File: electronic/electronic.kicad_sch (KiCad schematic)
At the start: 4 parts, among them M01 Brushless Motor, U1 ESC HW30A, U1 ESP32-DEVKITC-32E, U2 MPU-6050

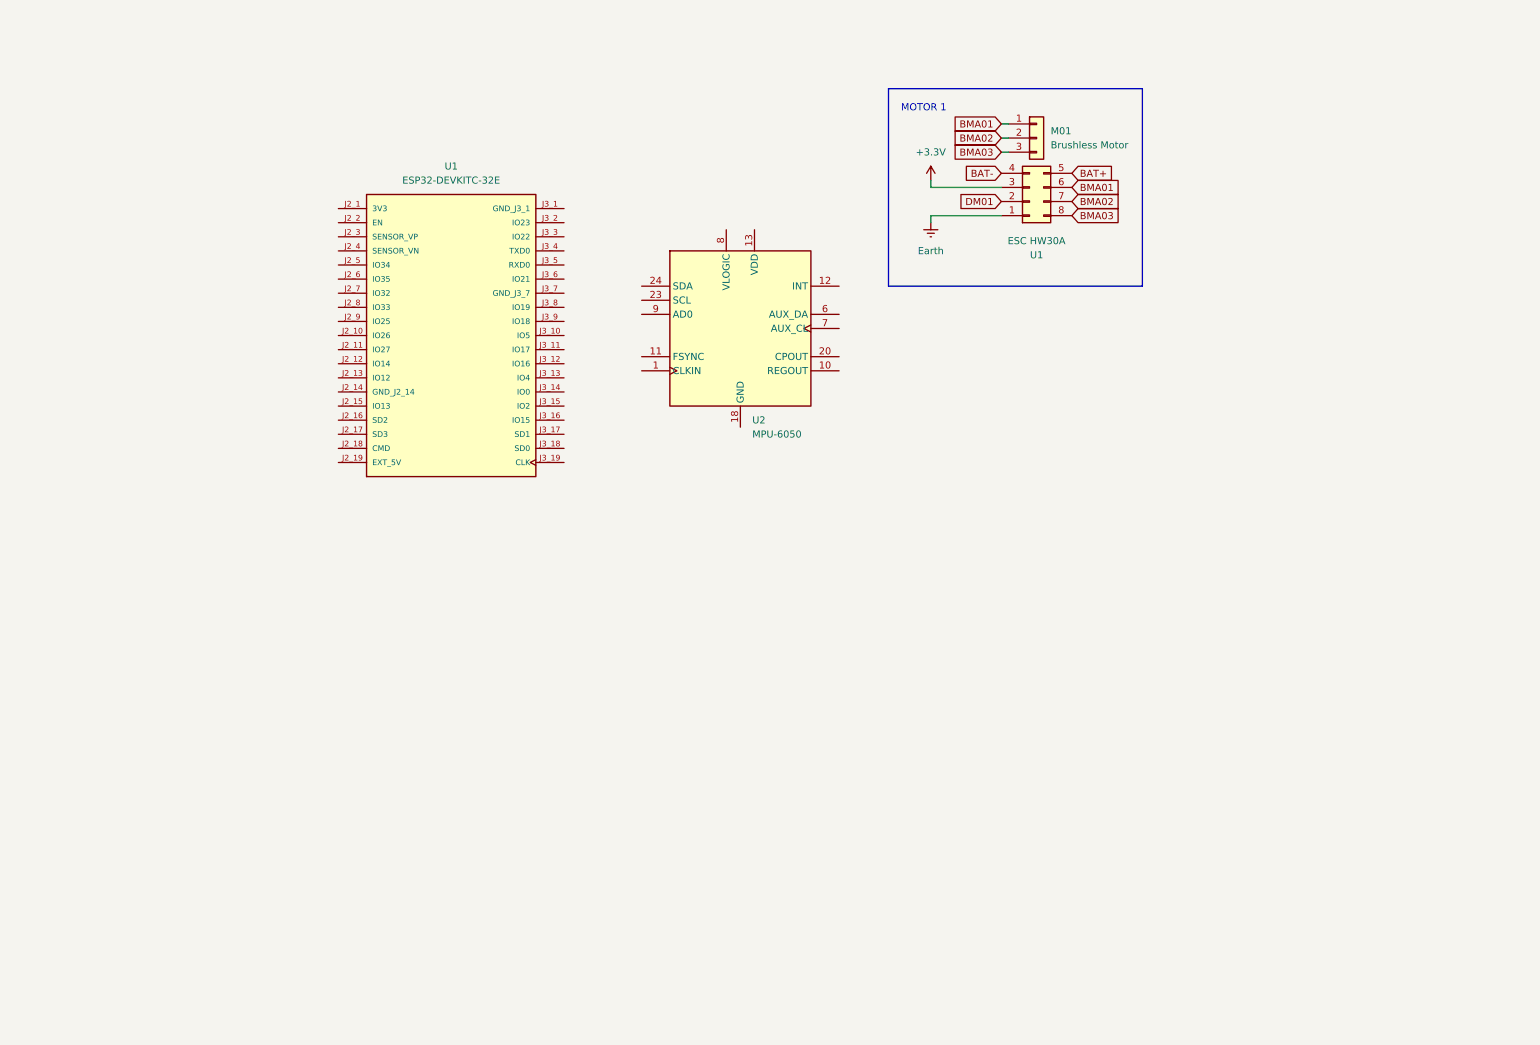
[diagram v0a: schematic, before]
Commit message: feat: motors, DHT11 and BMP280 added to electronic schematic
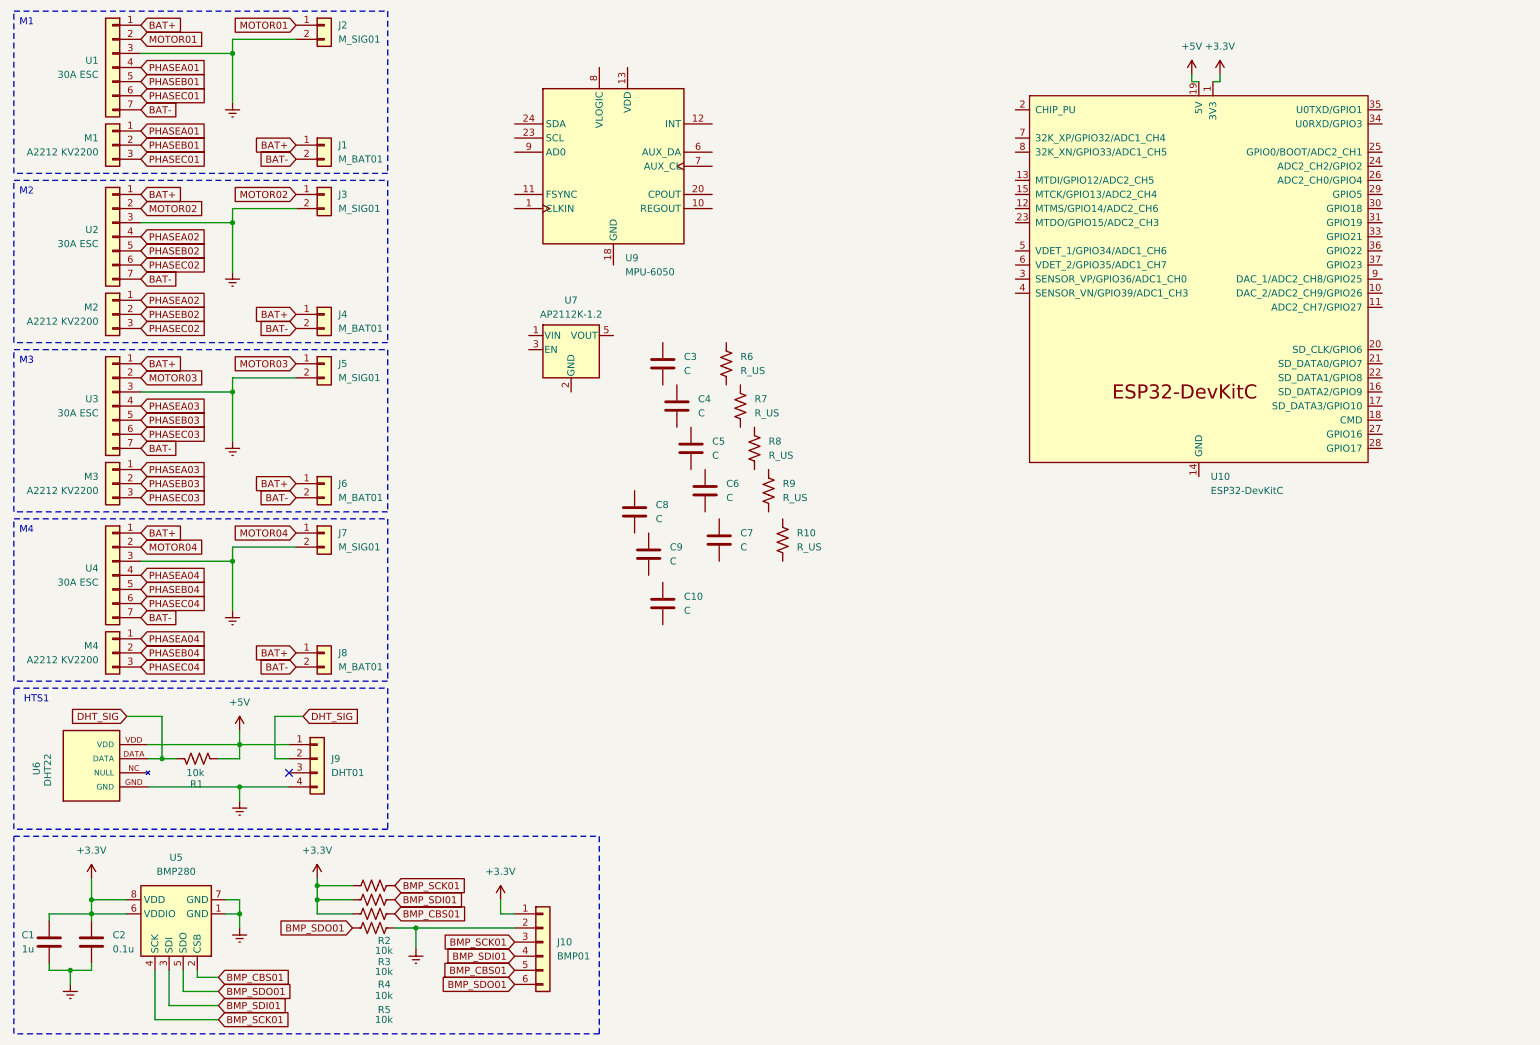
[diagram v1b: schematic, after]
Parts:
- removed M01: Brushless Motor, symbol Connector_Generic:Conn_01x03
- removed U1: ESP32-DEVKITC-32E, ESP32-DEVKITC-32E:MODULE_ESP32-DEVKITC-32E, symbol ESP32-DEVKITC-32E:ESP32-DEVKITC-32E
- removed U1: ESC HW30A, symbol Connector_Generic:Conn_02x04_Counter_Clockwise
- removed U2: MPU-6050, Sensor_Motion:InvenSense_QFN-24_4x4mm_P0.5mm, symbol Sensor_Motion:MPU-6050
- added C1: 1u, symbol Device:C
- added C10, C3, C4, C5, C6, C7, C8, C9: C, symbol Device:C
- added C2: 0.1u, symbol Device:C
- added J1, J4, J6, J8: M_BAT01, symbol Connector_Generic:Conn_01x02
- added J10: BMP01, symbol Connector_Generic:Conn_01x06
- added J2, J3, J5, J7: M_SIG01, symbol Connector_Generic:Conn_01x02
- added J9: DHT01, symbol Connector_Generic:Conn_01x04
- added M1, M2, M3, M4: A2212 KV2200, symbol Connector_Generic:Conn_01x03
- added R1, R2, R3, R4, R5: 10k, symbol Device:R_US
- added R10, R6, R7, R8, R9: R_US, symbol Device:R_US
- added U1, U2, U3, U4: 30A ESC, symbol Connector_Generic:Conn_01x07
- added U10: ESP32-DevKitC, PCM_Espressif:ESP32-DevKitC, symbol PCM_Espressif:ESP32-DevKitC
- added U5: BMP280, Package_LGA:Bosch_LGA-8_2x2.5mm_P0.65mm_ClockwisePinNumbering, symbol Sensor_Pressure:BMP280
- added U6: DHT22, DHT22:DHT22, symbol DHT22:DHT22
- added U7: AP2112K-1.2, Package_TO_SOT_SMD:SOT-23-5, symbol Regulator_Linear:AP2112K-1.2
- added U9: MPU-6050, Sensor_Motion:InvenSense_QFN-24_4x4mm_P0.5mm, symbol Sensor_Motion:MPU-6050
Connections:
- net +3.3V: now also C1.1, C2.1, J10.1 (Pin_1), R2.1, R3.1, R4.1, U10.1 (3V3), U5.6 (VDDIO), U5.8 (VDD)
- net BAT+: now also J1.1 (Pin_1), J4.1 (Pin_1), J6.1 (Pin_1), J8.1 (Pin_1), U1.1 (Pin_1), U2.1 (Pin_1), U3.1 (Pin_1), U4.1 (Pin_1)
- net BAT-: now also J1.2 (Pin_2), J4.2 (Pin_2), J6.2 (Pin_2), J8.2 (Pin_2), U1.7 (Pin_7), U2.7 (Pin_7), U3.7 (Pin_7), U4.7 (Pin_7)
- net Earth: now also C1.2, C2.2, J10.2 (Pin_2), J2.2 (Pin_2), J3.2 (Pin_2), J5.2 (Pin_2), J7.2 (Pin_2), J9.4 (Pin_4), R5.2, U1.3 (Pin_3), U2.3 (Pin_3), U3.3 (Pin_3), U4.3 (Pin_3), U5.1 (GND), U5.7 (GND), U6.GND
- new net: U10.14 (GND), U10.32 (GND), U10.38 (GND)
- new net +5V: J9.1 (Pin_1), R1.1, U10.19 (5V), U6.VDD
- new net BMP_CBS01: J10.5 (Pin_5), R4.2, U5.2 (CSB)
- new net BMP_SCK01: J10.3 (Pin_3), R2.2, U5.4 (SCK)
- new net BMP_SDI01: J10.4 (Pin_4), R3.2, U5.3 (SDI)
- new net BMP_SDO01: J10.6 (Pin_6), R5.1, U5.5 (SDO)
- new net DHT_SIG: J9.2 (Pin_2), R1.2, U6.DATA
- new net MOTOR01: J2.1 (Pin_1), U1.2 (Pin_2)
- new net MOTOR02: J3.1 (Pin_1), U2.2 (Pin_2)
- new net MOTOR03: J5.1 (Pin_1), U3.2 (Pin_2)
- new net MOTOR04: J7.1 (Pin_1), U4.2 (Pin_2)
- new net PHASEA01: M1.1 (Pin_1), U1.4 (Pin_4)
- new net PHASEA02: M2.1 (Pin_1), U2.4 (Pin_4)
- new net PHASEA03: M3.1 (Pin_1), U3.4 (Pin_4)
- new net PHASEA04: M4.1 (Pin_1), U4.4 (Pin_4)
- new net PHASEB01: M1.2 (Pin_2), U1.5 (Pin_5)
- new net PHASEB02: M2.2 (Pin_2), U2.5 (Pin_5)
- new net PHASEB03: M3.2 (Pin_2), U3.5 (Pin_5)
- new net PHASEB04: M4.2 (Pin_2), U4.5 (Pin_5)
- new net PHASEC01: M1.3 (Pin_3), U1.6 (Pin_6)
- new net PHASEC02: M2.3 (Pin_3), U2.6 (Pin_6)
- new net PHASEC03: M3.3 (Pin_3), U3.6 (Pin_6)
- new net PHASEC04: M4.3 (Pin_3), U4.6 (Pin_6)
- no-connect marks 0 -> 1
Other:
- note added: "HTS1"
- note added: "M1"
- note added: "M2"
- note added: "M3"
- note added: "M4"
- note removed: "MOTOR 1"

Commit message: feat: MPU6050, NEO-6M and OLED display added to electronic schematic
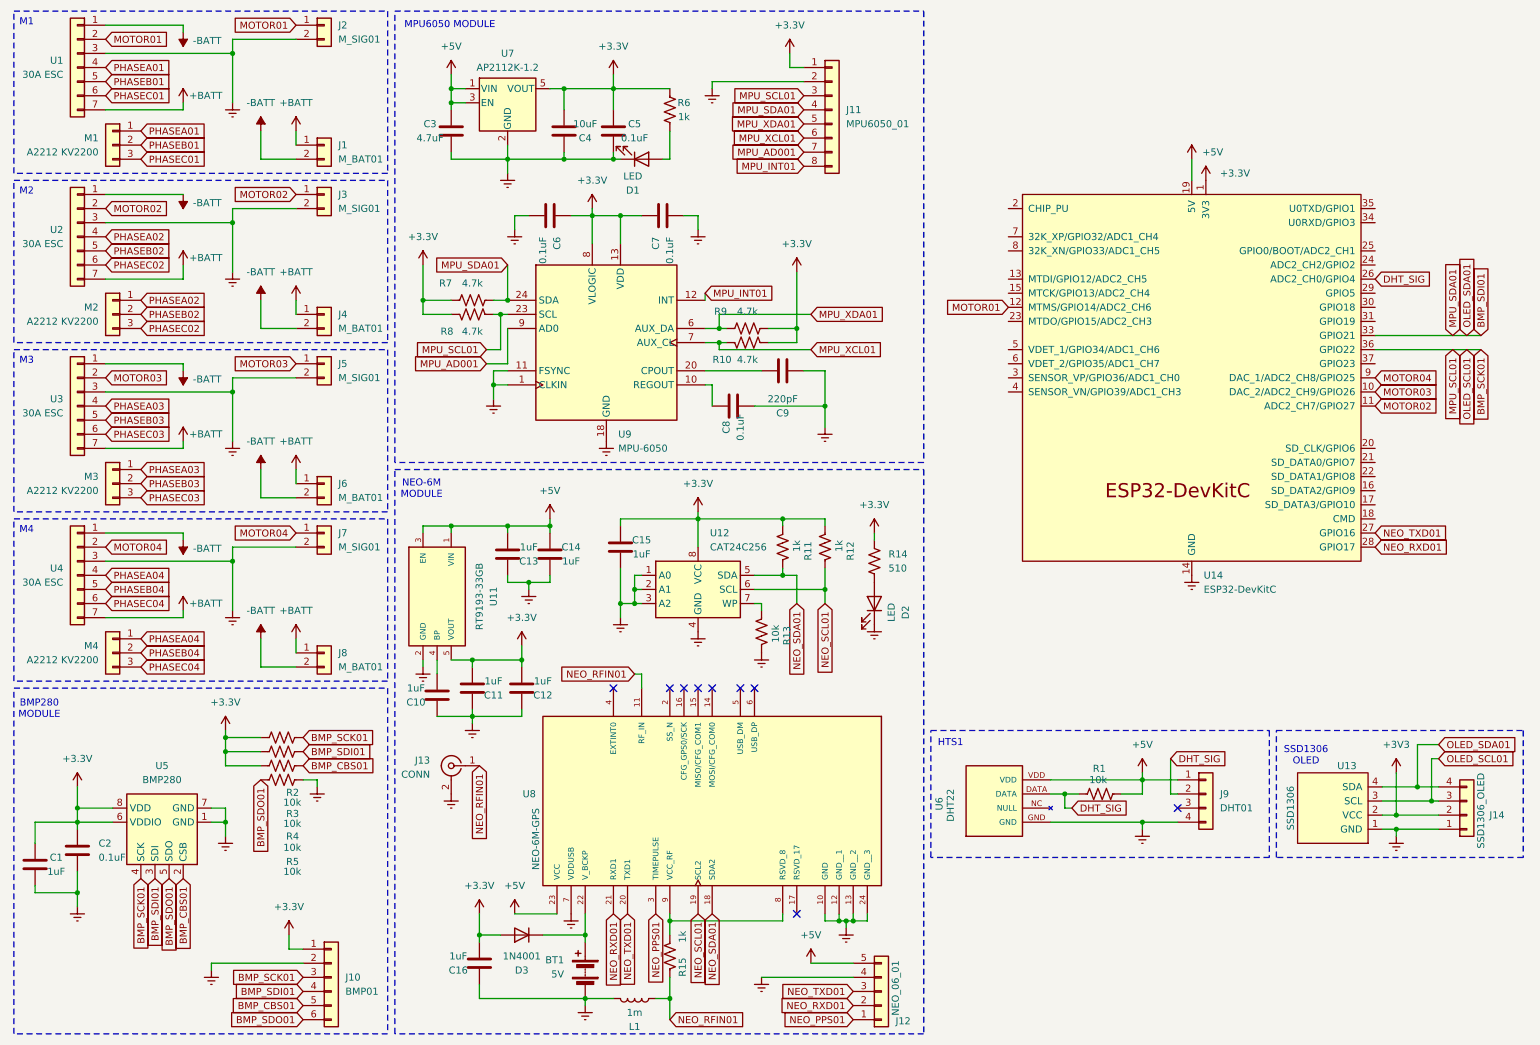
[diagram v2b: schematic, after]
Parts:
- removed U10: ESP32-DevKitC, PCM_Espressif:ESP32-DevKitC, symbol PCM_Espressif:ESP32-DevKitC
- added BT1: 5V, symbol Device:Battery
- added C11, C12, C13, C14, C15, C16: 1uF, symbol Device:C
- added D1, D2: LED, LED_SMD:LED_0402_1005Metric, symbol Device:LED
- added D3: 1N4001, Diode_THT:D_DO-41_SOD81_P10.16mm_Horizontal, symbol Diode:1N4001
- added J11: MPU6050_01, symbol Connector_Generic:Conn_01x08
- added J12: NEO_06_01, symbol Connector_Generic:Conn_01x05
- added J13: CONN, symbol Connector:Conn_Coaxial
- added J14: SSD1306_OLED, symbol Connector_Generic:Conn_01x04
- added L1: 1m, symbol Device:L
- added R11, R12, R15: 1k, symbol Device:R_US
- added R13: 10k, symbol Device:R_US
- added R14: 510, symbol Device:R_US
- added U11: RT9193-33GB, RT9193-33GB:SOT23-5_TEXAS_INSTRUMETNS, symbol RT9193-33GB:RT9193-33GB
- added U12: CAT24C256, symbol Memory_EEPROM:CAT24C256
- added U13: SSD1306, symbol custom:SSD1306
- added U14: ESP32-DevKitC, RF_Module:ESP32-S2-WROVER, symbol PCM_Espressif:ESP32-DevKitC
- added U8: NEO-6M-GPS, NEO-6M-GPS:XCVR_NEO-6M-GPS, symbol NEO-6M-GPS:NEO-6M-GPS
- C1: value 1u -> 1uF
- C10: value C -> 1uF
- C2: value 0.1u -> 0.1uF
- C3: value C -> 4.7uF
- C4: value C -> 10uF
- C5, C6, C7, C8: value C -> 0.1uF
- C9: value C -> 220pF
- R10, R7, R8, R9: value R_US -> 4.7k
- R6: value R_US -> 1k
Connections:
- net +3.3V: now also C4.2, C5.1, C6.1, C7.1, R10.2, R6.1, R7.1, R8.1, R9.2, U7.5 (VOUT), U9.13 (VDD), U9.8 (VLOGIC), C11.2, C12.2, C15.1, C16.2, D3.2 (A), J11.1 (Pin_1), R11.1, R12.1, R14.2, U11.5 (VOUT), U12.8 (VCC), U14.1 (3V3)
- net +5V: now also C3.1, U7.1 (VIN), U7.3 (EN), C13.2, C14.1, J12.5 (Pin_5), U11.1 (VIN), U11.3 (EN), U14.19 (5V), U8.23 (VCC)
- net BMP_SCK01: now also R8.2, U9.23 (SCL), J11.3 (Pin_3), J14.3 (Pin_3), U13.3 (SCL), U14.36 (GPIO22)
- net BMP_SDI01: now also R7.2, U9.24 (SDA), J11.4 (Pin_4), J14.4 (Pin_4), U13.4 (SDA), U14.33 (GPIO21)
- net DHT_SIG: now also U14.26 (ADC2_CH0/GPIO4)
- net Earth: now also C10.1, C3.2, C4.1, C5.2, C6.2, C7.2, C8.2, C9.2, U7.2 (GND), U9.1 (CLKIN), U9.11 (FSYNC), U9.18 (GND), BT1.2 (-), C11.1, C12.1, C13.1, C14.2, C15.2, C16.1, D1.1 (K), D2.1 (K), J11.2 (Pin_2), J12.4 (Pin_4), J13.2 (Ext), J14.1 (Pin_1), L1.2, R13.2, U11.2 (GND), U12.1 (A0), U12.2 (A1), U12.3 (A2), U12.4 (GND), U13.1 (GND), U14.14 (GND), U14.32 (GND), U14.38 (GND), U8.10 (GND), U8.12 (GND__1), U8.13 (GND__2), U8.24 (GND__3), U8.7 (VDDUSB)
- net MOTOR01: now also U14.12 (MTMS/GPIO14/ADC2_CH6)
- net MOTOR02: now also U14.11 (ADC2_CH7/GPIO27)
- net MOTOR03: now also U14.10 (DAC_2/ADC2_CH9/GPIO26)
- net MOTOR04: now also U14.9 (DAC_1/ADC2_CH8/GPIO25)
- net at C10.2: now also U11.4 (BP)
- net MPU_XCL01: now reaches R10.1
- net MPU_XCL01: now also U9.7 (AUX_CL), J11.6 (Pin_6)
- net at C8.1: now also U9.10 (REGOUT)
- net at C9.1: now also U9.20 (CPOUT)
- net MPU_XDA01: now reaches R9.1
- net MPU_XDA01: now also U9.6 (AUX_DA), J11.5 (Pin_5)
- net MPU_INT01: now reaches U9.12 (INT)
- net MPU_INT01: now also J11.8 (Pin_8)
- net MPU_AD001: now reaches U9.9 (AD0)
- net MPU_AD001: now also J11.7 (Pin_7)
- net at R6.2: now also D1.2 (A)
- net BAT+ renamed +BATT
- net +BATT: now also U1.7 (Pin_7), U2.7 (Pin_7), U3.7 (Pin_7), U4.7 (Pin_7); no longer U1.1 (Pin_1), U2.1 (Pin_1), U3.1 (Pin_1), U4.1 (Pin_1)
- net BAT- renamed -BATT
- net -BATT: now also U1.1 (Pin_1), U2.1 (Pin_1), U3.1 (Pin_1), U4.1 (Pin_1); no longer U1.7 (Pin_7), U2.7 (Pin_7), U3.7 (Pin_7), U4.7 (Pin_7)
- new net: R15.1, U8.8 (RSVD_8), U8.9 (VCC_RF)
- new net: BT1.1 (+), D3.1 (K), U8.22 (V_BCKP)
- new net: R13.1, U12.7 (WP)
- new net: D2.2 (A), R14.1
- new net +3V3: J14.2 (Pin_2), U13.2 (VCC)
- new net NEO_PPS01: J12.1 (Pin_1), U8.3 (TIMEPULSE)
- new net NEO_RFIN01: J13.1 (In), L1.1, R15.2, U8.11 (RF_IN)
- new net NEO_RXD01: J12.2 (Pin_2), U14.28 (GPIO17), U8.21 (RXD1)
- new net NEO_SCL01: R12.2, U12.6 (SCL), U8.19 (SCL2)
- new net NEO_SDA01: R11.2, U12.5 (SDA), U8.18 (SDA2)
- new net NEO_TXD01: J12.3 (Pin_3), U14.27 (GPIO16), U8.20 (TXD1)
- no-connect marks 1 -> 9
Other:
- note added: "BMP280 MODULE"
- note added: "MPU6050 MODULE"
- note added: "NEO-6M MODULE"
- note added: "SSD1306 OLED"
- title: (none) -> Squematico de la plataforma
- moved on the sheet: C1, C2, C3, C4, C5, C6, C7, C8, C9, J10, J9, R1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
